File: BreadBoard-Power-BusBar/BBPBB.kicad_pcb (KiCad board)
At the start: 4 copper layers, 53.6 x 5.2 mm, 2 parts, among them J1 Conn_02x02_Odd_Even, J2 Conn_02x02_Odd_Even

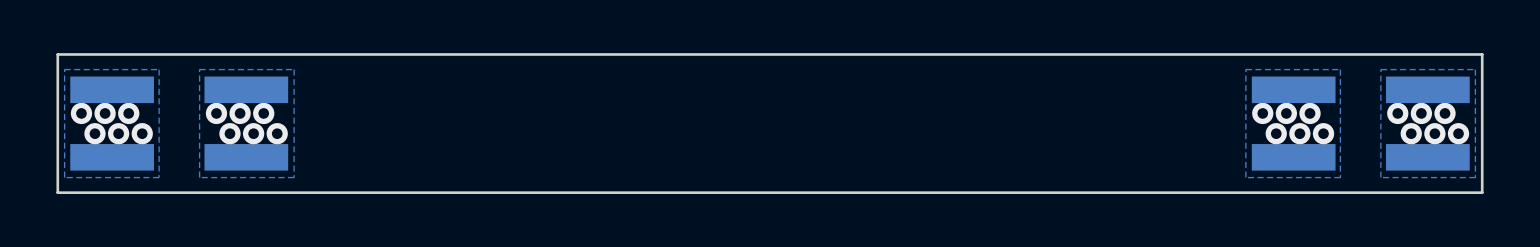
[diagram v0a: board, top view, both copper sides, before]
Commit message: Moved the headers by about 0.5 mm.
The previous distance was too small and the headers didn't fit properly into the breadboard.
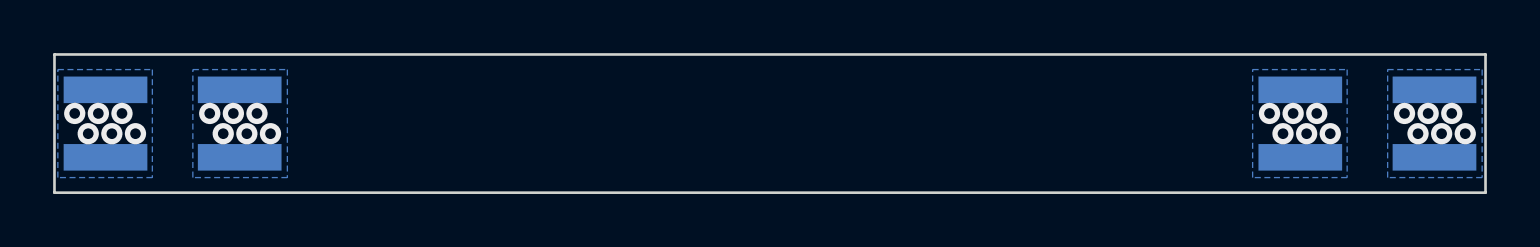
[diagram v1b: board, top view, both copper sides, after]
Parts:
- moved J2 0.25 mm to (149.5, 127.0)
- moved J1 0.25 mm to (104.5, 127.0)
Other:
- board size 53.6 x 5.2 mm -> 53.8 x 5.2 mm
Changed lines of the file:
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@@
   )
   (module Connector_PinHeader_2.54mm:PinHeader_2x02_P2.54mm_Vertical_SMD (layer B.Cu)
-    (at 104.77 127)
+    (at 104.521 127)
     (descr "surface-mounted straight pin header, 2x02, 2.54mm pitch, double rows")
     (tags "Surface mounted pin header SMD 2x02 2.54mm double row")
@@
   )
   (module Connector_PinHeader_2.54mm:PinHeader_2x02_P2.54mm_Vertical_SMD (layer B.Cu)
-    (at 149.23 127)
+    (at 149.479 127)
     (descr "surface-mounted straight pin header, 2x02, 2.54mm pitch, double rows")
     (tags "Surface mounted pin header SMD 2x02 2.54mm double row")
@@
     (effects (font (size 1.016 1.016) (thickness 0.1524)))
   )
-  (gr_line (start 100.2 124.4) (end 153.8 124.4) (layer Edge.Cuts) (width 0.1))
-  (gr_line (start 153.8 129.6) (end 100.2 129.6) (layer Edge.Cuts) (width 0.1))
-  (gr_line (start 153.8 124.4) (end 153.8 129.6) (layer Edge.Cuts) (width 0.1))
-  (gr_line (start 100.2 124.4) (end 100.2 129.6) (layer Edge.Cuts) (width 0.1))
-  (via (at 101.6 127.381) (size 0.8) (drill 0.4) (layers F.Cu B.Cu) (net 1))
-  (via (at 101.092 126.619) (size 0.8) (drill 0.4) (layers F.Cu B.Cu) (net 1))
-  (via (at 102.87 126.619) (size 0.8) (drill 0.4) (layers F.Cu B.Cu) (net 1))
-  (via (at 102.489 127.381) (size 0.8) (drill 0.4) (layers F.Cu B.Cu) (net 1))
-  (via (at 103.378 127.381) (size 0.8) (drill 0.4) (layers F.Cu B.Cu) (net 1))
-  (via (at 101.981 126.619) (size 0.8) (drill 0.4) (layers F.Cu B.Cu) (net 1))
-  (via (at 106.68 127.381) (size 0.8) (drill 0.4) (layers F.Cu B.Cu) (net 2))
-  (via (at 106.172 126.619) (size 0.8) (drill 0.4) (layers F.Cu B.Cu) (net 2))
-  (via (at 107.95 126.619) (size 0.8) (drill 0.4) (layers F.Cu B.Cu) (net 2))
-  (via (at 107.569 127.381) (size 0.8) (drill 0.4) (layers F.Cu B.Cu) (net 2))
-  (via (at 108.458 127.381) (size 0.8) (drill 0.4) (layers F.Cu B.Cu) (net 2))
-  (via (at 107.061 126.619) (size 0.8) (drill 0.4) (layers F.Cu B.Cu) (net 2))
-  (via (at 146.05 127.381) (size 0.8) (drill 0.4) (layers F.Cu B.Cu) (net 1))
-  (via (at 145.542 126.619) (size 0.8) (drill 0.4) (layers F.Cu B.Cu) (net 1))
-  (via (at 147.32 126.619) (size 0.8) (drill 0.4) (layers F.Cu B.Cu) (net 1))
-  (via (at 146.939 127.381) (size 0.8) (drill 0.4) (layers F.Cu B.Cu) (net 1))
-  (via (at 147.828 127.381) (size 0.8) (drill 0.4) (layers F.Cu B.Cu) (net 1))
-  (via (at 146.431 126.619) (size 0.8) (drill 0.4) (layers F.Cu B.Cu) (net 1))
-  (via (at 150.622 126.619) (size 0.8) (drill 0.4) (layers F.Cu B.Cu) (net 2))
-  (via (at 151.13 127.381) (size 0.8) (drill 0.4) (layers F.Cu B.Cu) (net 2))
-  (via (at 151.511 126.619) (size 0.8) (drill 0.4) (layers F.Cu B.Cu) (net 2))
-  (via (at 152.019 127.381) (size 0.8) (drill 0.4) (layers F.Cu B.Cu) (net 2))
-  (via (at 152.4 126.619) (size 0.8) (drill 0.4) (layers F.Cu B.Cu) (net 2))
-  (via (at 152.908 127.381) (size 0.8) (drill 0.4) (layers F.Cu B.Cu) (net 2))
+  (gr_line (start 100.076 124.4) (end 153.924 124.4) (layer Edge.Cuts) (width 0.1))
+  (gr_line (start 153.924 129.6) (end 100.076 129.6) (layer Edge.Cuts) (width 0.1))
+  (gr_line (start 153.924 124.4) (end 153.924 129.6) (layer Edge.Cuts) (width 0.1))
+  (gr_line (start 100.076 124.4) (end 100.076 129.6) (layer Edge.Cuts) (width 0.1))
+  (via (at 101.346 127.381) (size 0.8) (drill 0.4) (layers F.Cu B.Cu) (net 1))
+  (via (at 100.838 126.619) (size 0.8) (drill 0.4) (layers F.Cu B.Cu) (net 1))
+  (via (at 102.616 126.619) (size 0.8) (drill 0.4) (layers F.Cu B.Cu) (net 1))
+  (via (at 102.235 127.381) (size 0.8) (drill 0.4) (layers F.Cu B.Cu) (net 1))
+  (via (at 103.124 127.381) (size 0.8) (drill 0.4) (layers F.Cu B.Cu) (net 1))
+  (via (at 101.727 126.619) (size 0.8) (drill 0.4) (layers F.Cu B.Cu) (net 1))
+  (via (at 146.304 127.381) (size 0.8) (drill 0.4) (layers F.Cu B.Cu) (net 1))
+  (via (at 145.796 126.619) (size 0.8) (drill 0.4) (layers F.Cu B.Cu) (net 1))
+  (via (at 147.574 126.619) (size 0.8) (drill 0.4) (layers F.Cu B.Cu) (net 1))
+  (via (at 147.193 127.381) (size 0.8) (drill 0.4) (layers F.Cu B.Cu) (net 1))
+  (via (at 148.082 127.381) (size 0.8) (drill 0.4) (layers F.Cu B.Cu) (net 1))
+  (via (at 146.685 126.619) (size 0.8) (drill 0.4) (layers F.Cu B.Cu) (net 1))
+  (via (at 106.426 127.381) (size 0.8) (drill 0.4) (layers F.Cu B.Cu) (net 2))
+  (via (at 105.918 126.619) (size 0.8) (drill 0.4) (layers F.Cu B.Cu) (net 2))
+  (via (at 107.696 126.619) (size 0.8) (drill 0.4) (layers F.Cu B.Cu) (net 2))
+  (via (at 107.315 127.381) (size 0.8) (drill 0.4) (layers F.Cu B.Cu) (net 2))
+  (via (at 108.204 127.381) (size 0.8) (drill 0.4) (layers F.Cu B.Cu) (net 2))
+  (via (at 106.807 126.619) (size 0.8) (drill 0.4) (layers F.Cu B.Cu) (net 2))
+  (via (at 150.876 126.619) (size 0.8) (drill 0.4) (layers F.Cu B.Cu) (net 2))
+  (via (at 151.384 127.381) (size 0.8) (drill 0.4) (layers F.Cu B.Cu) (net 2))
+  (via (at 151.765 126.619) (size 0.8) (drill 0.4) (layers F.Cu B.Cu) (net 2))
+  (via (at 152.273 127.381) (size 0.8) (drill 0.4) (layers F.Cu B.Cu) (net 2))
+  (via (at 152.654 126.619) (size 0.8) (drill 0.4) (layers F.Cu B.Cu) (net 2))
+  (via (at 153.162 127.381) (size 0.8) (drill 0.4) (layers F.Cu B.Cu) (net 2))
   (zone (net 2) (net_name /Power-1) (layer In1.Cu) (hatch edge 0.508)
     (connect_pads yes (clearance 0.508))
@@
     (polygon
       (pts
-        (xy 153.543 129.032) (xy 149.987 129.032) (xy 149.987 124.968) (xy 153.543 124.968)
+        (xy 153.797 129.032) (xy 150.241 129.032) (xy 150.241 124.968) (xy 153.797 124.968)
       )
     )
@@
     (polygon
       (pts
-        (xy 148.463 129.032) (xy 144.907 129.032) (xy 144.907 124.968) (xy 148.463 124.968)
+        (xy 148.717 129.032) (xy 145.161 129.032) (xy 145.161 124.968) (xy 148.717 124.968)
       )
     )
@@
     (polygon
       (pts
-        (xy 109.093 129.032) (xy 105.537 129.032) (xy 105.537 124.968) (xy 109.093 124.968)
+        (xy 108.839 129.032) (xy 105.283 129.032) (xy 105.283 124.968) (xy 108.839 124.968)
       )
     )
@@
     (polygon
       (pts
-        (xy 104.013 129.032) (xy 100.457 129.032) (xy 100.457 124.968) (xy 104.013 124.968)
-      )
-    )
+        (xy 103.759 129.032) (xy 100.203 129.032) (xy 100.203 124.968) (xy 103.759 124.968)
+      )
+    )

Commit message: Added some decals...
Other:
- board text added: "Breadboard Power Busbar"
- board text added: "Rev. 20/2"
- board text added: "http://michis-pla.net"
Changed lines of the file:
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@@
   (general
     (thickness 1.6)
-    (drawings 9)
+    (drawings 12)
     (tracks 24)
     (zones 0)
@@
     (tags "Surface mounted pin header SMD 2x02 2.54mm double row")
     (attr smd)
-    (fp_text reference J1 (at 0 3.6) (layer B.SilkS)
+    (fp_text reference J1 (at 5.715 0) (layer B.SilkS)
       (effects (font (size 1 1) (thickness 0.15)) (justify mirror))
     )
@@
     (tags "Surface mounted pin header SMD 2x02 2.54mm double row")
     (attr smd)
-    (fp_text reference J2 (at 0 3.6) (layer B.SilkS)
+    (fp_text reference J2 (at -5.715 0) (layer B.SilkS)
       (effects (font (size 1 1) (thickness 0.15)) (justify mirror))
     )
@@
     )
   )
+  (gr_text "Breadboard Power Busbar" (at 127 127) (layer F.SilkS)
+    (effects (font (size 1.27 1.27) (thickness 0.254)))
+  )
+  (gr_text "Rev.\n20/2" (at 116.967 127) (layer B.SilkS)
+    (effects (font (size 0.8 0.8) (thickness 0.1)) (justify left mirror))
+  )
+  (gr_text http://michis-pla.net (at 130.429 127) (layer B.SilkS)
+    (effects (font (size 1.27 1.27) (thickness 0.254)) (justify mirror))
+  )
   (gr_line (start 103.5 126.5) (end 103.5 127.5) (layer Cmts.User) (width 0.01))

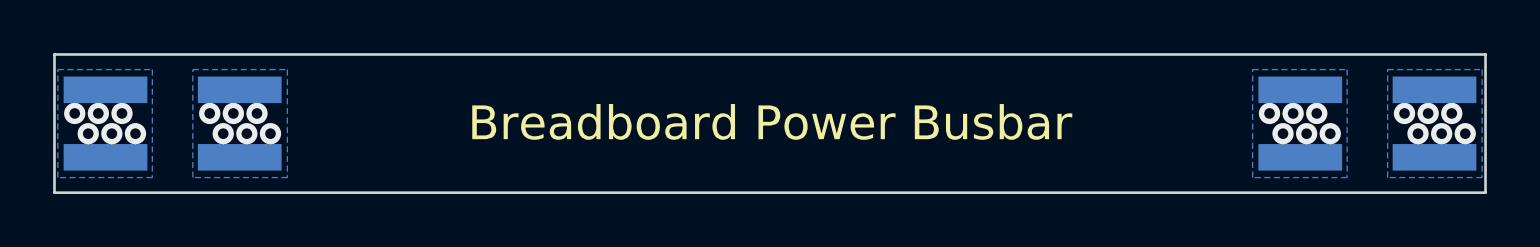
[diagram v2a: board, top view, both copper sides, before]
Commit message: Finished placing and routing the new components for the Power indication.
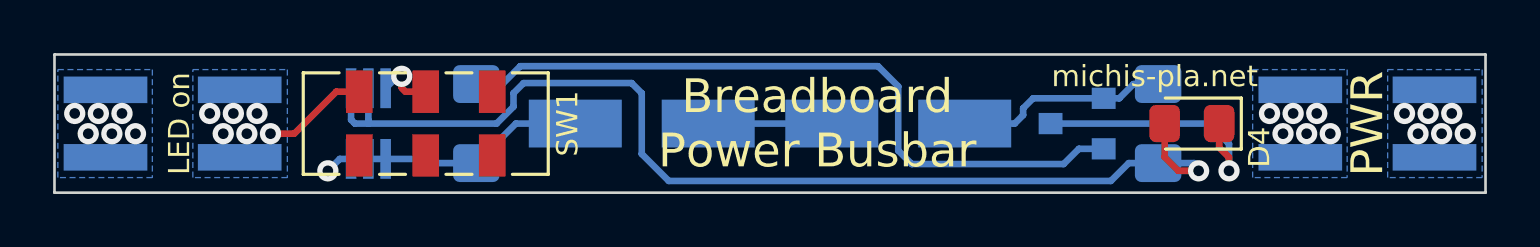
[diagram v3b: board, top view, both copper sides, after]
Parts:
- added D1: BAS40BRW, Package_TO_SOT_SMD:SOT-363_SC-70-6_Handsoldering, B.Cu at (111.9, 127.0)
- added D2: S1B, Diode_SMD:D_SMA_Handsoldering, B.Cu at (131.8, 127.0)
- added D3: S1B, Diode_SMD:D_SMA_Handsoldering, B.Cu at (122.2, 127.0)
- added D4: Everlight 17-21SYGC, LED_SMD:LED_0805_2012Metric_Pad1.15x1.40mm_HandSolder, F.Cu at (142.9, 127.0)
- added Q1: BC847B, Package_TO_SOT_SMD:SOT-23, B.Cu at (138.6, 127.0)
- added R1: 1k, Resistor_SMD:R_1206_3216Metric_Pad1.42x1.75mm_HandSolder, B.Cu at (141.6, 127.0)
- added R2: 150, Resistor_SMD:R_1206_3216Metric_Pad1.42x1.75mm_HandSolder, B.Cu at (116.0, 127.0)
- added SW1: JS102011JCQN, mibe:SW_DPDT_CK_JS202011JCQN, F.Cu at (114.0, 127.0)
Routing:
- net VCC: track 0.00 -> 41.6 mm, vias 0 -> 1
- net Net-(Q1-Pad2): track 0.00 -> 27.1 mm
- net Net-(D4-Pad1): track 0.00 -> 9.98 mm, vias 0 -> 1
- net GND: track 0.00 -> 8.47 mm
- net Net-(D2-Pad2): track 0.00 -> 8.05 mm
- net Net-(D2-Pad1): track 0.00 -> 4.65 mm
- net /Power-1: track 0.00 -> 4.00 mm
- net Net-(D1-Pad6): track 0.00 -> 2.19 mm, vias 0 -> 1
- net /Power-2: track 0.00 -> 1.06 mm, vias 12 -> 13
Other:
- board text added: "LED on"
- board text added: "PWR"
- board text added: "michis-pla.net"
- board text removed: "Rev. 20/2"
- board text removed: "http://michis-pla.net"

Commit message: Added OSWH Logo on the silkscreen layer.
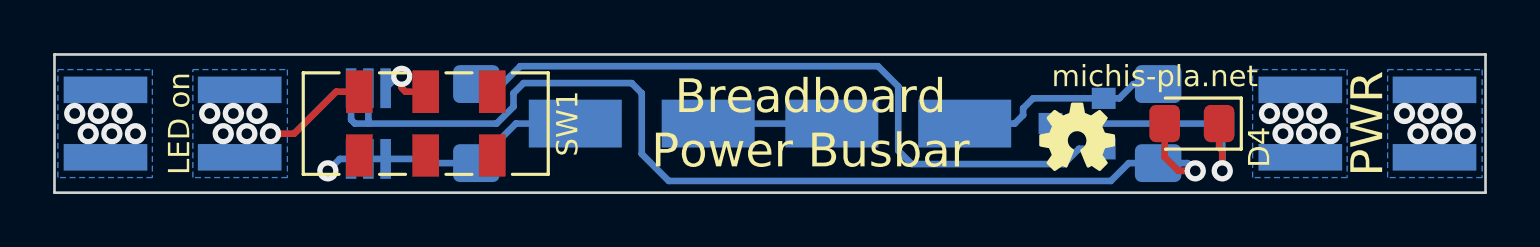
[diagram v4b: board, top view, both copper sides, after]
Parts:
- added REF**: OSHW-Logo_2.7x2.5mm_SilkScreen_NoText, mibe:OSHW-Logo_2.7x2.5mm_SilkScreen_NoText, F.Cu at (138.6, 127.6)
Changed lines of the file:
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@@
     (thickness 1.6)
     (drawings 13)
-    (tracks 88)
+    (tracks 87)
     (zones 0)
-    (modules 10)
+    (modules 11)
     (nets 11)
   )
@@
     (1 In1.Cu signal hide)
     (2 In2.Cu signal hide)
-    (31 B.Cu signal hide)
+    (31 B.Cu signal)
     (34 B.Paste user hide)
     (35 F.Paste user)
@@
     (solder_mask_min_width 0.02)
     (aux_axis_origin 0 0)
-    (visible_elements 7FFFFBFF)
+    (visible_elements 7FFFFFFF)
     (pcbplotparams
       (layerselection 0x010fc_ffffffff)
@@
     (add_net "Net-(SW1-Pad1)")
     (add_net VCC)
+  )
+  (module mibe:OSHW-Logo_2.7x2.5mm_SilkScreen_NoText (layer F.Cu)
+    (at 138.557 127.635)
+    (descr "Imported from c:\\Users\\Michi\\Desktopaa\\oshw-logo.svg")
+    (tags svg2mod)
+    (attr virtual)
+    (fp_text reference REF** (at 0 0) (layer F.SilkS) hide
+      (effects (font (size 1 1) (thickness 0.15)))
+    )
+    (fp_text value OSHW-Logo_2.7x2.5mm_SilkScreen_NoText (at 0 0) (layer F.Fab) hide
+      (effects (font (size 1 1) (thickness 0.15)))
+    )
+    (fp_poly (pts (xy 1.373638 -0.193721) (xy 1.032614 -0.257139) (xy 1.02046 -0.263416) (xy 1.012429 -0.274496)
+      (xy 0.907896 -0.51837) (xy 0.905459 -0.531745) (xy 0.909555 -0.544723) (xy 1.108249 -0.834322)
+      (xy 1.11119 -0.846467) (xy 1.106071 -0.857897) (xy 0.857901 -1.106068) (xy 0.846494 -1.111194)
+      (xy 0.834356 -1.108185) (xy 0.539676 -0.905963) (xy 0.526656 -0.901823) (xy 0.513185 -0.904111)
+      (xy 0.276777 -1.000901) (xy 0.265645 -1.008753) (xy 0.259351 -1.020851) (xy 0.193694 -1.373575)
+      (xy 0.187196 -1.384257) (xy 0.175501 -1.388709) (xy -0.175501 -1.388709) (xy -0.187178 -1.384267)
+      (xy -0.193673 -1.373575) (xy -0.25931 -1.020851) (xy -0.265595 -1.008753) (xy -0.276735 -1.000901)
+      (xy -0.513164 -0.904127) (xy -0.526651 -0.901878) (xy -0.539655 -0.905979) (xy -0.834314 -1.1082)
+      (xy -0.846478 -1.11116) (xy -0.85788 -1.106084) (xy -1.106071 -0.857913) (xy -1.111197 -0.846492)
+      (xy -1.108248 -0.834338) (xy -0.909534 -0.544738) (xy -0.905471 -0.531751) (xy -0.907896 -0.518386)
+      (xy -1.01245 -0.274512) (xy -1.020457 -0.263402) (xy -1.032635 -0.257155) (xy -1.373638 -0.193737)
+      (xy -1.384326 -0.1872) (xy -1.38876 -0.175507) (xy -1.388739 0.175473) (xy -1.384297 0.187184)
+      (xy -1.373616 0.193677) (xy -1.040974 0.255578) (xy -1.028929 0.261892) (xy -1.021225 0.273067)
+      (xy -0.917376 0.532481) (xy -0.915164 0.545972) (xy -0.919347 0.558971) (xy -1.108291 0.834317)
+      (xy -1.111231 0.846472) (xy -1.106113 0.857892) (xy -0.857902 1.106063) (xy -0.8465 1.11116)
+      (xy -0.834336 1.10818) (xy -0.563865 0.922535) (xy -0.551016 0.918725) (xy -0.537934 0.921741)
+      (xy -0.418651 0.985426) (xy -0.399048 0.978203) (xy -0.153097 0.383928) (xy -0.152778 0.371535)
+      (xy -0.160317 0.361703) (xy -0.190168 0.34342) (xy -0.209046 0.328974) (xy -0.228804 0.315448)
+      (xy -0.247661 0.300761) (xy -0.265565 0.284966) (xy -0.282466 0.268114) (xy -0.29831 0.250255)
+      (xy -0.313047 0.23144) (xy -0.326626 0.211722) (xy -0.338994 0.19115) (xy -0.3501 0.169777)
+      (xy -0.359893 0.147654) (xy -0.368321 0.12483) (xy -0.375332 0.101359) (xy -0.380874 0.077291)
+      (xy -0.384897 0.052676) (xy -0.387349 0.027568) (xy -0.388177 0.002015) (xy -0.387414 -0.022533)
+      (xy -0.385153 -0.046675) (xy -0.38144 -0.070366) (xy -0.376322 -0.09356) (xy -0.369843 -0.116212)
+      (xy -0.362048 -0.138276) (xy -0.352984 -0.159708) (xy -0.342696 -0.18046) (xy -0.331229 -0.200489)
+      (xy -0.318628 -0.219748) (xy -0.30494 -0.238192) (xy -0.29021 -0.255775) (xy -0.274483 -0.272453)
+      (xy -0.257805 -0.288179) (xy -0.240221 -0.302909) (xy -0.221776 -0.316596) (xy -0.202517 -0.329196)
+      (xy -0.182488 -0.340662) (xy -0.161736 -0.350949) (xy -0.140305 -0.360013) (xy -0.118241 -0.367806)
+      (xy -0.09559 -0.374285) (xy -0.072397 -0.379403) (xy -0.048708 -0.383115) (xy -0.024567 -0.385376)
+      (xy -0.000022 -0.386139) (xy 0.024524 -0.385376) (xy 0.048664 -0.383115) (xy 0.072353 -0.379403)
+      (xy 0.095546 -0.374285) (xy 0.118196 -0.367806) (xy 0.140259 -0.360013) (xy 0.161689 -0.350949)
+      (xy 0.18244 -0.340662) (xy 0.202468 -0.329196) (xy 0.221726 -0.316596) (xy 0.240169 -0.302909)
+      (xy 0.257752 -0.288179) (xy 0.274429 -0.272453) (xy 0.290155 -0.255775) (xy 0.304884 -0.238192)
+      (xy 0.318571 -0.219748) (xy 0.33117 -0.200489) (xy 0.342636 -0.18046) (xy 0.352924 -0.159708)
+      (xy 0.361987 -0.138276) (xy 0.369781 -0.116212) (xy 0.376259 -0.09356) (xy 0.381377 -0.070366)
+      (xy 0.385089 -0.046675) (xy 0.38735 -0.022533) (xy 0.388113 0.002015) (xy 0.387285 0.027568)
+      (xy 0.384834 0.052676) (xy 0.380812 0.077291) (xy 0.37527 0.101359) (xy 0.368261 0.12483)
+      (xy 0.359835 0.147654) (xy 0.350043 0.169777) (xy 0.338938 0.19115) (xy 0.326571 0.211722)
+      (xy 0.312993 0.23144) (xy 0.298255 0.250255) (xy 0.28241 0.268114) (xy 0.265509 0.284966)
+      (xy 0.247603 0.300761) (xy 0.228743 0.315448) (xy 0.208982 0.328974) (xy 0.190146 0.34342)
+      (xy 0.160294 0.361703) (xy 0.15278 0.371535) (xy 0.153075 0.383928) (xy 0.399005 0.978224)
+      (xy 0.418608 0.985447) (xy 0.537891 0.921762) (xy 0.550981 0.918806) (xy 0.563822 0.922556)
+      (xy 0.834314 1.108201) (xy 0.846467 1.111141) (xy 0.857859 1.106084) (xy 1.10607 0.857913)
+      (xy 1.111204 0.846483) (xy 1.108248 0.834339) (xy 0.919283 0.558992) (xy 0.915127 0.545997)
+      (xy 0.917333 0.532502) (xy 1.021182 0.273086) (xy 1.028875 0.261881) (xy 1.04091 0.255597)
+      (xy 1.373553 0.193695) (xy 1.384226 0.187163) (xy 1.388677 0.175492) (xy 1.388718 -0.175491)
+      (xy 1.384297 -0.187206) (xy 1.373637 -0.193721) (xy 1.373638 -0.193721)) (layer F.SilkS) (width 0.078406))
   )
   (module Package_TO_SOT_SMD:SOT-23 (layer B.Cu)
@@
     (effects (font (size 0.8 0.8) (thickness 0.1)))
   )
-  (gr_text "Breadboard\nPower Busbar" (at 128.778 127) (layer F.SilkS)
+  (gr_text "Breadboard\nPower Busbar" (at 128.524 127) (layer F.SilkS)
     (effects (font (size 1.27 1.27) (thickness 0.254)))
   )
@@
   (segment (start 113.142 125.222) (end 113.142 125.658) (width 0.25) (layer F.Cu) (net 3))
   (segment (start 113.142 125.658) (end 113.284 125.8) (width 0.25) (layer F.Cu) (net 3))
-  (via (at 143.129 128.778) (size 0.8) (drill 0.4) (layers F.Cu B.Cu) (net 4))
   (segment (start 111.887 125.67) (end 111.887 127) (width 0.25) (layer B.Cu) (net 4) (status 400000))
   (segment (start 111.887 127) (end 111.887 126.873) (width 0.25) (layer B.Cu) (net 4))
-  (segment (start 143.129 128.778) (end 143.129 128.651) (width 0.25) (layer B.Cu) (net 4))
-  (segment (start 142.9655 128.4875) (end 141.605 128.4875) (width 0.25) (layer B.Cu) (net 4))
-  (segment (start 143.129 128.651) (end 142.9655 128.4875) (width 0.25) (layer B.Cu) (net 4))
-  (segment (start 143.129 128.778) (end 142.367 128.778) (width 0.25) (layer F.Cu) (net 4))
-  (segment (start 141.85 128.261) (end 141.85 127) (width 0.25) (layer F.Cu) (net 4))
-  (segment (start 142.367 128.778) (end 141.85 128.261) (width 0.25) (layer F.Cu) (net 4))
   (segment (start 140.4985 128.4875) (end 141.605 128.4875) (width 0.25) (layer B.Cu) (net 4))
   (segment (start 139.827 129.159) (end 140.4985 128.4875) (width 0.25) (layer B.Cu) (net 4))
@@
   (segment (start 122.174 128.143) (end 123.19 129.159) (width 0.25) (layer B.Cu) (net 4))
   (segment (start 123.19 129.159) (end 139.827 129.159) (width 0.25) (layer B.Cu) (net 4))
+  (segment (start 141.85 128.261) (end 141.85 127) (width 0.25) (layer F.Cu) (net 4))
+  (segment (start 143.002 128.778) (end 142.7115 128.4875) (width 0.25) (layer B.Cu) (net 4))
+  (via (at 143.002 128.778) (size 0.8) (drill 0.4) (layers F.Cu B.Cu) (net 4))
+  (segment (start 143.002 128.778) (end 142.367 128.778) (width 0.25) (layer F.Cu) (net 4))
+  (segment (start 142.7115 128.4875) (end 141.605 128.4875) (width 0.25) (layer B.Cu) (net 4))
+  (segment (start 142.367 128.778) (end 141.85 128.261) (width 0.25) (layer F.Cu) (net 4))
   (segment (start 119.674 127) (end 117.4385 127) (width 0.25) (layer B.Cu) (net 5) (status 400000))
   (segment (start 117.4385 127) (end 115.951 128.4875) (width 0.25) (layer B.Cu) (net 5) (status 800000))
@@
   (segment (start 140.142 126.05) (end 140.6795 125.5125) (width 0.25) (layer B.Cu) (net 6))
   (segment (start 124.674 127) (end 129.326 127) (width 0.25) (layer B.Cu) (net 7) (status C00000))
-  (via (at 144.272 128.778) (size 0.8) (drill 0.4) (layers F.Cu B.Cu) (net 8))
-  (segment (start 137.557 127) (end 143.51 127) (width 0.25) (layer B.Cu) (net 8))
-  (segment (start 144.272 127.762) (end 144.272 128.778) (width 0.25) (layer B.Cu) (net 8))
-  (segment (start 143.51 127) (end 144.272 127.762) (width 0.25) (layer B.Cu) (net 8))
   (segment (start 143.9 127.898) (end 143.9 127) (width 0.25) (layer F.Cu) (net 8))
-  (segment (start 144.272 128.778) (end 144.272 128.27) (width 0.25) (layer F.Cu) (net 8))
-  (segment (start 144.272 128.27) (end 143.9 127.898) (width 0.25) (layer F.Cu) (net 8))
+  (segment (start 144.018 128.016) (end 143.9 127.898) (width 0.25) (layer F.Cu) (net 8))
+  (segment (start 144.018 128.778) (end 144.018 127.508) (width 0.25) (layer B.Cu) (net 8))
+  (via (at 144.018 128.778) (size 0.8) (drill 0.4) (layers F.Cu B.Cu) (net 8))
+  (segment (start 144.018 127.508) (end 143.51 127) (width 0.25) (layer B.Cu) (net 8))
+  (segment (start 143.51 127) (end 137.557 127) (width 0.25) (layer B.Cu) (net 8))
+  (segment (start 144.018 128.778) (end 144.018 128.016) (width 0.25) (layer F.Cu) (net 8))
   (segment (start 138.623 127.95) (end 139.557 127.95) (width 0.25) (layer B.Cu) (net 9))
   (segment (start 138.049 128.524) (end 138.623 127.95) (width 0.25) (layer B.Cu) (net 9))
